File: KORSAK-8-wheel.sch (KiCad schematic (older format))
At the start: 16 parts, among them J1 Screw_Terminal_01x04, J2 Conn_01x02_Male, J3 Screw_Terminal_01x06, J4 Screw_Terminal_01x04, M1 Motor_DC, M2 Motor_DC, M3 Motor_DC, M4 Motor_DC, M5 Motor_DC, M6 Motor_DC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

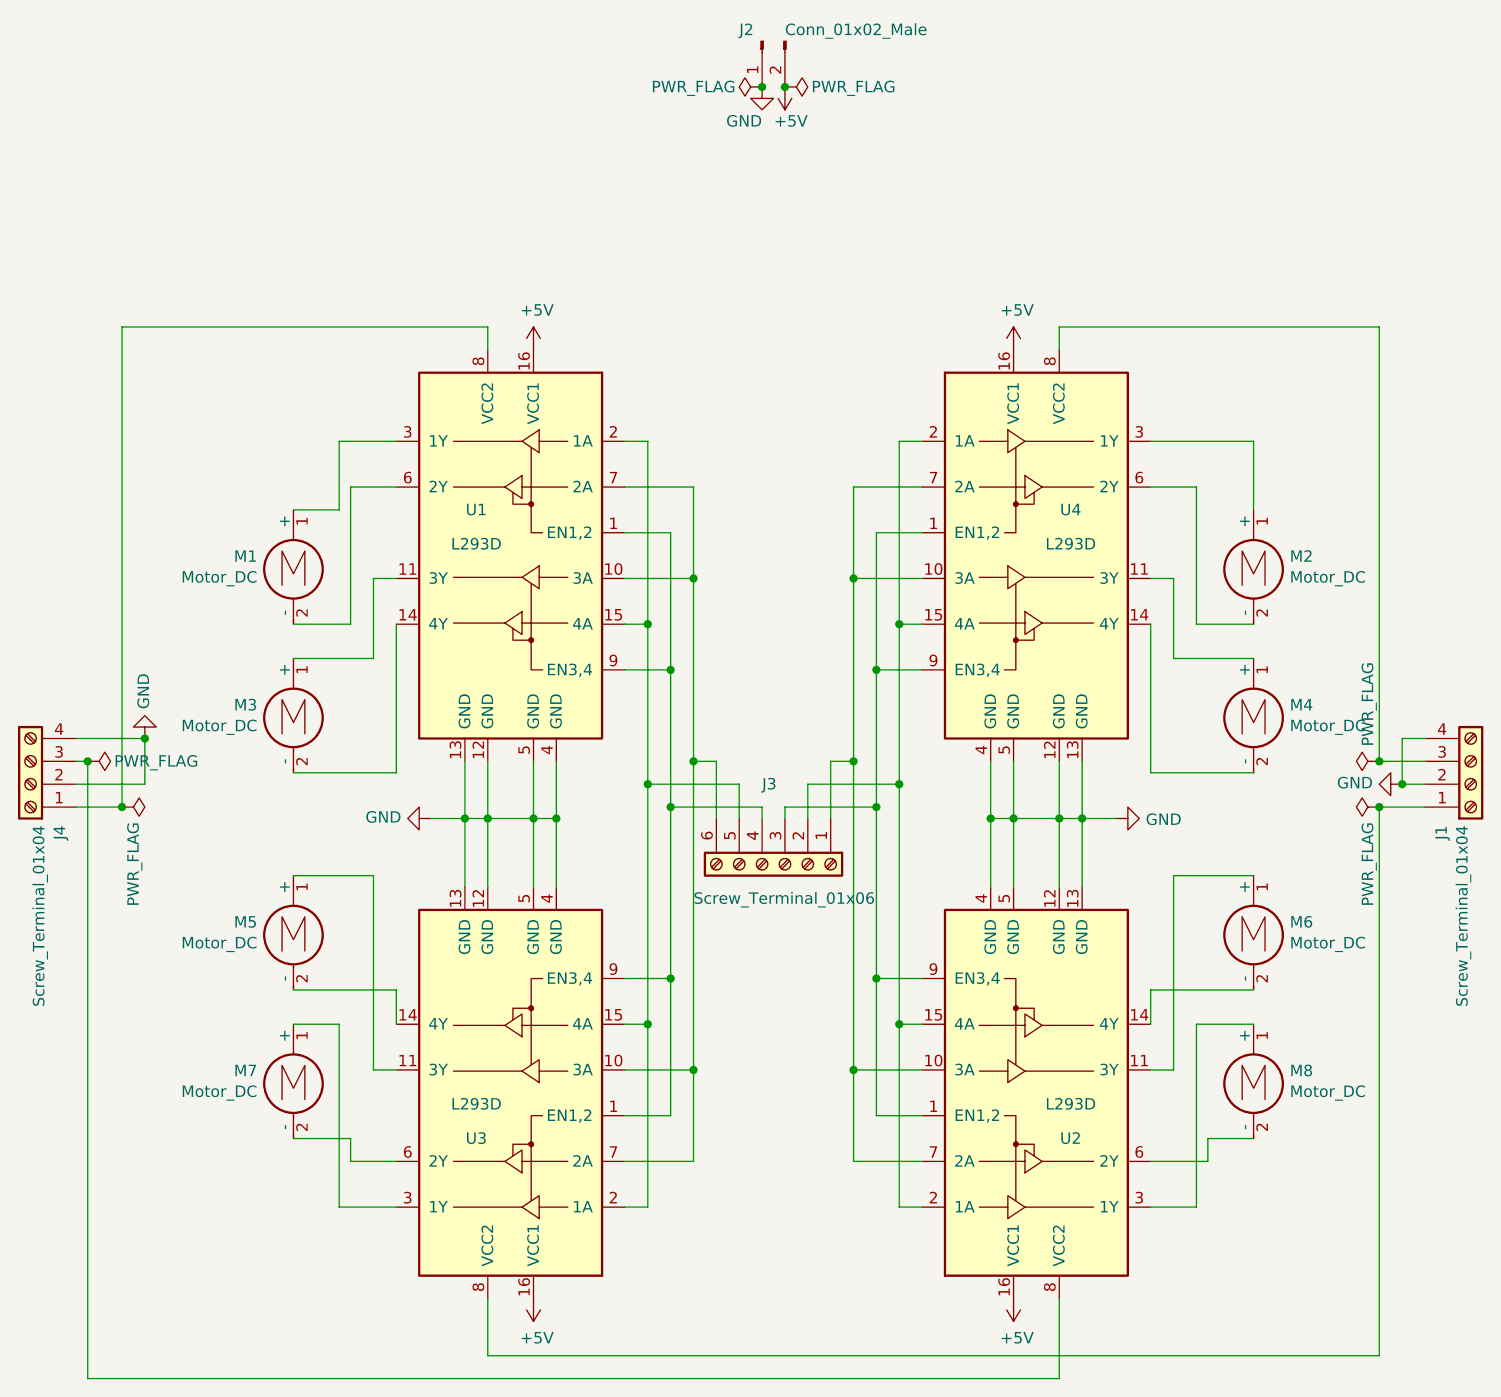
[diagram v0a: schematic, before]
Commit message: Исправил обозначения двигателей в схеме
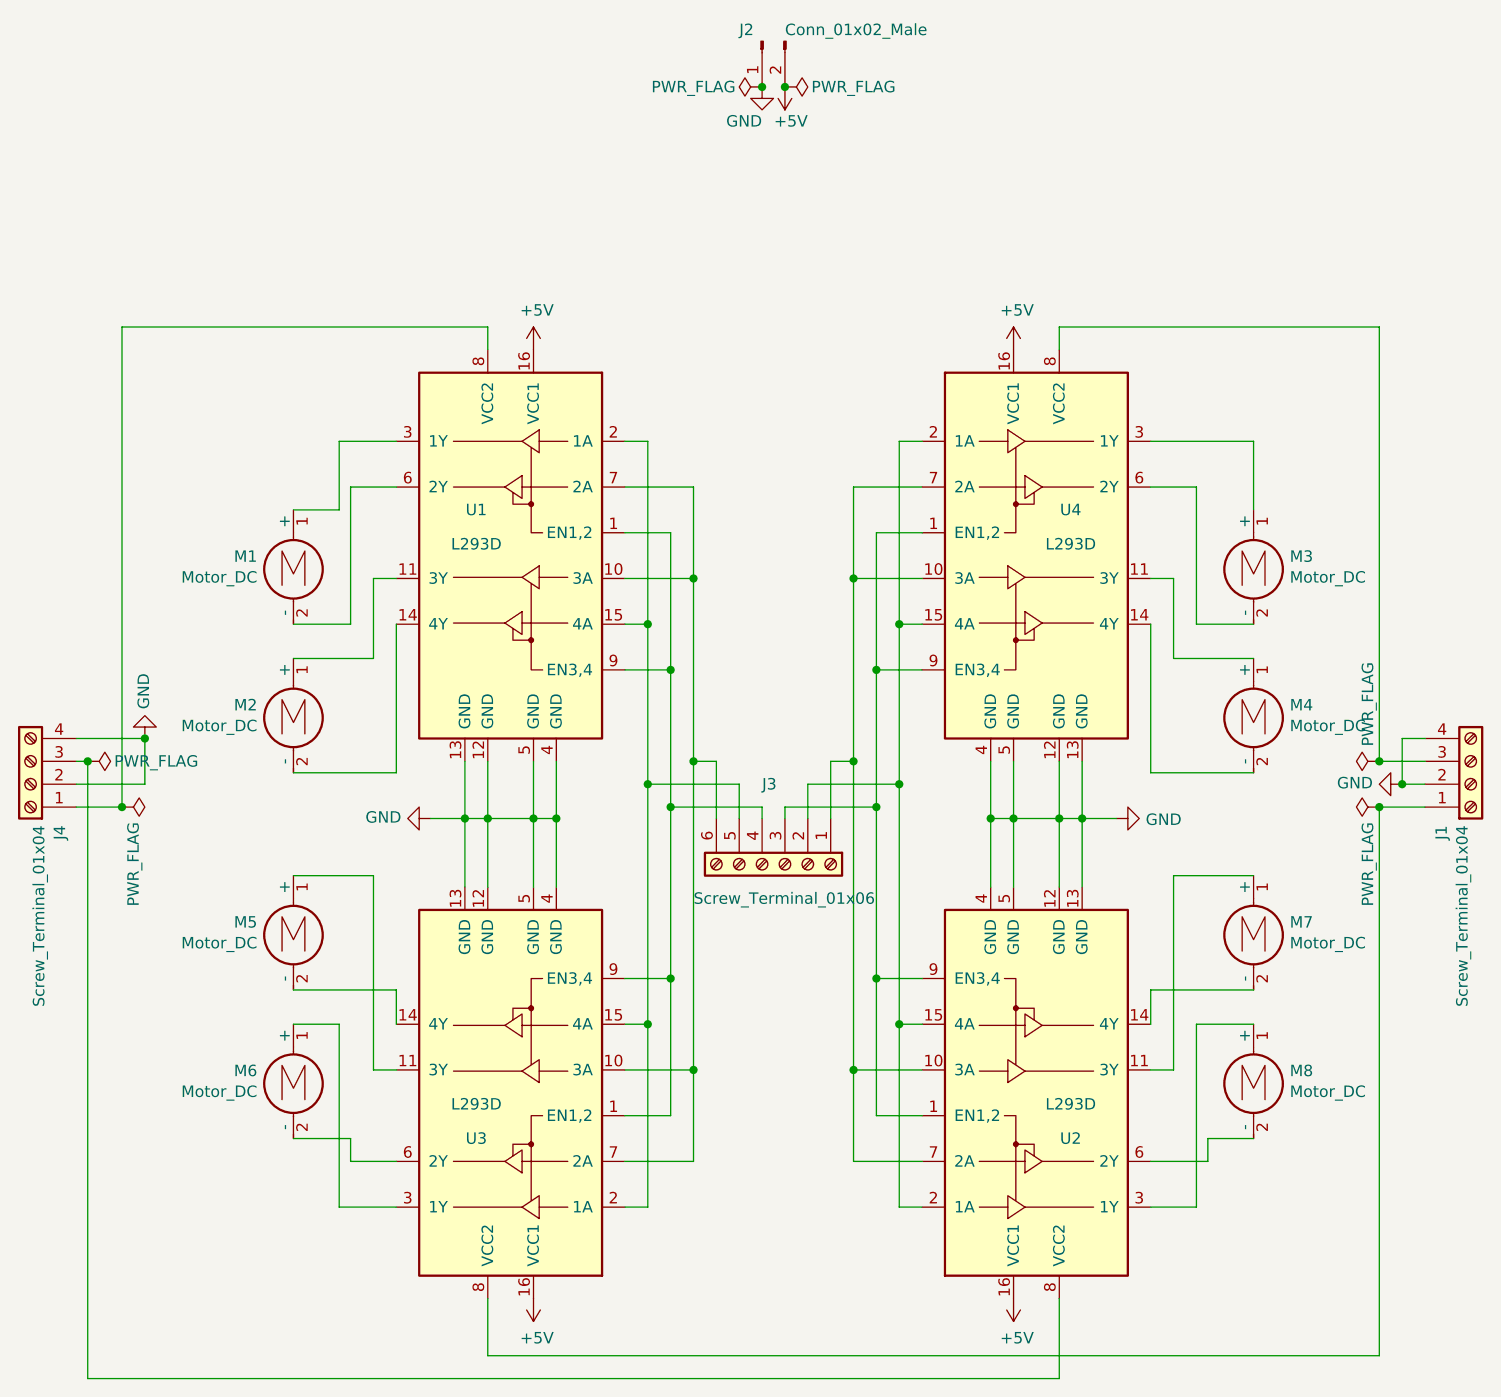
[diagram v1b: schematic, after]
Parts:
- renumbered M3 to M2, M2 to M3, M7 to M6, M6 to M7
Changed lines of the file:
@@
 $EndComp
 $Comp
-L Motor:Motor_DC M2
+L Motor:Motor_DC M3
 U 1 1 5F9B5F4B
 P 6300 3550
-F 0 "M2" H 6458 3546 50  0000 L CNN
+F 0 "M3" H 6458 3546 50  0000 L CNN
 F 1 "Motor_DC" H 6458 3455 50  0000 L CNN
 F 2 "TerminalBlock_Phoenix:TerminalBlock_Phoenix_MKDS-1,5-2_1x02_P5.00mm_Horizontal" H 6300 3460 50  0001 C CNN
@@
 $EndComp
 $Comp
-L Motor:Motor_DC M3
+L Motor:Motor_DC M2
 U 1 1 6010707E
 P 2100 4200
-F 0 "M3" H 2258 4196 50  0000 L CNN
+F 0 "M2" H 2258 4196 50  0000 L CNN
 F 1 "Motor_DC" H 2258 4105 50  0000 L CNN
 F 2 "TerminalBlock_Phoenix:TerminalBlock_Phoenix_MKDS-1,5-2_1x02_P5.00mm_Horizontal" H 2100 4110 50  0001 C CNN
@@
 $EndComp
 $Comp
-L Motor:Motor_DC M6
+L Motor:Motor_DC M7
 U 1 1 601FA1A6
 P 6300 5150
-F 0 "M6" H 6458 5146 50  0000 L CNN
+F 0 "M7" H 6458 5146 50  0000 L CNN
 F 1 "Motor_DC" H 6458 5055 50  0000 L CNN
 F 2 "TerminalBlock_Phoenix:TerminalBlock_Phoenix_MKDS-1,5-2_1x02_P5.00mm_Horizontal" H 6300 5060 50  0001 C CNN
@@
 $EndComp
 $Comp
-L Motor:Motor_DC M7
+L Motor:Motor_DC M6
 U 1 1 601FA1F2
 P 2100 5800
-F 0 "M7" H 2258 5796 50  0000 L CNN
+F 0 "M6" H 2258 5796 50  0000 L CNN
 F 1 "Motor_DC" H 2258 5705 50  0000 L CNN
 F 2 "TerminalBlock_Phoenix:TerminalBlock_Phoenix_MKDS-1,5-2_1x02_P5.00mm_Horizontal" H 2100 5710 50  0001 C CNN
